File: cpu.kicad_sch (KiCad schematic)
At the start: 32 parts, among them J10 Skedd, J13 Boot, J7 USB_C_Receptacle_16P, U4 STM32H503KBUx

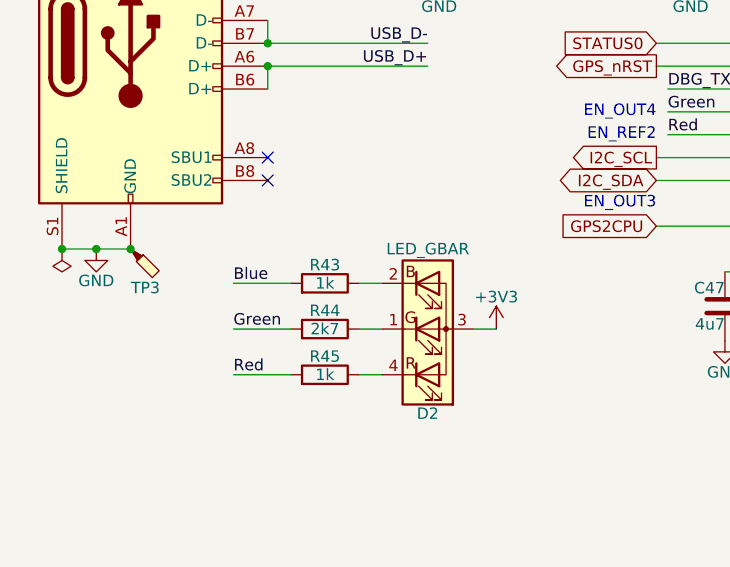
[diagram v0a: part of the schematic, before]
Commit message: Make all the LED resistors 0603 & adjust values.
Move the LED inwards so it doesn't overhang.
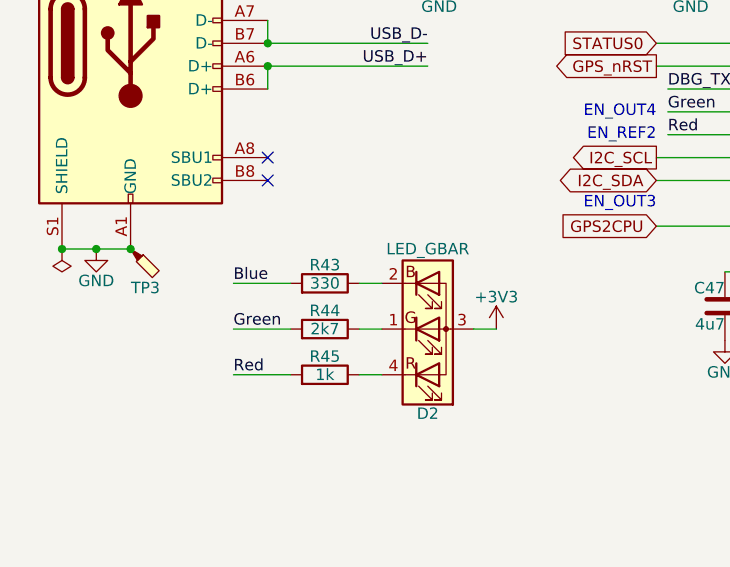
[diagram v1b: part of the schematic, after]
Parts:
- R43: value 1k -> 330; footprint Resistor_SMD:R_0402_1005Metric -> Resistor_SMD:R_0603_1608Metric; LCSC C11702 -> C23138
- R45: footprint Resistor_SMD:R_0402_1005Metric -> Resistor_SMD:R_0603_1608Metric; LCSC C11702 -> C21190

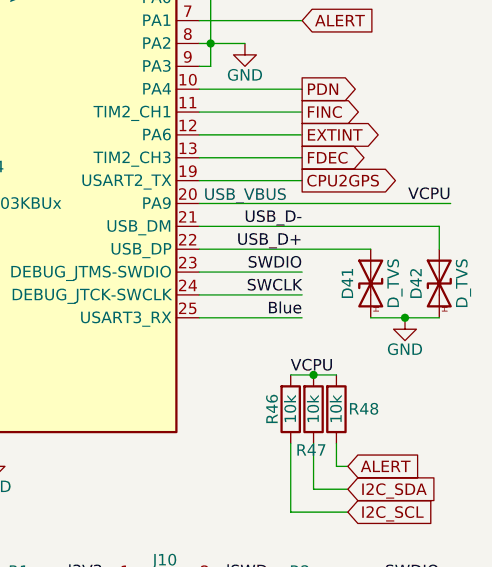
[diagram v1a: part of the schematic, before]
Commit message: Add LCSC part numbers for a few items.
Don't 'exclude from BOM' things we want to assemble.
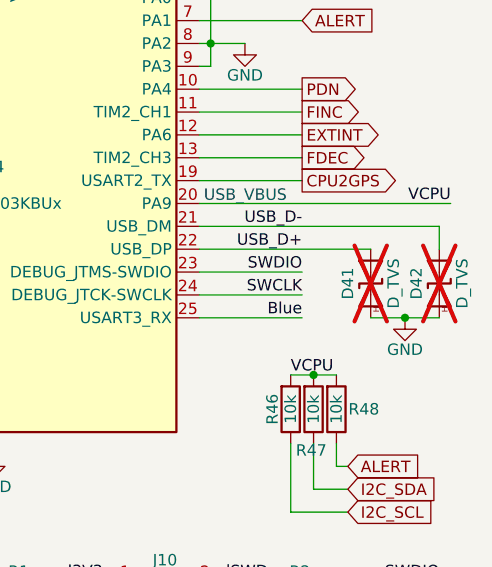
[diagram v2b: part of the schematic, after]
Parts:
- D41, D42: now not fitted
- J7: LCSC (none) -> C2765186; now in the parts list
- U4: now in the parts list

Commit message: Tweaks to python scripts.
Add part numbers for the LED and 470nF C0G capacitor.
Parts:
- D2: LCSC (none) -> C284951

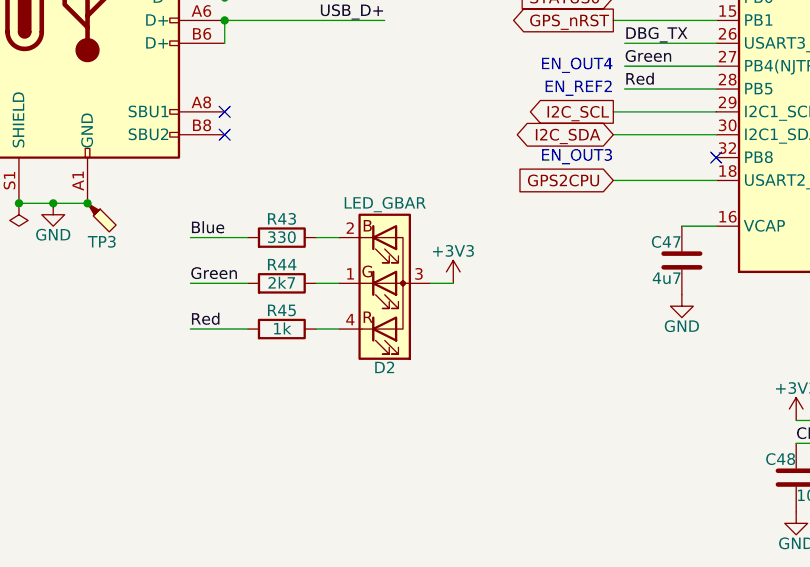
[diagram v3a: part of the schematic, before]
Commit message: Instead, switch to a RGB LED footprint from Paul Elliot.
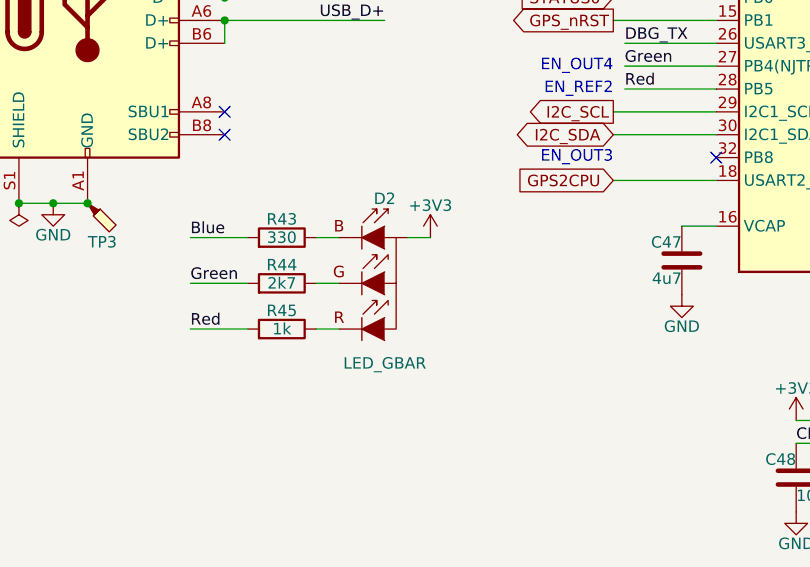
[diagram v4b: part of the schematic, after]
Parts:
- D2: footprint Parts:LED-QPLB615-RGB -> Parts:LED_RGB_SIDE; symbol Device:LED_GBAR -> Parts:LED_RGB_SIDE; LCSC C284951 -> C389528; now in the parts list
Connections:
- net +3V3: now also D2.1 (C); no longer D2.3 (A)
- net at R44.1: now also D2.3 (G); no longer D2.1 (GK)

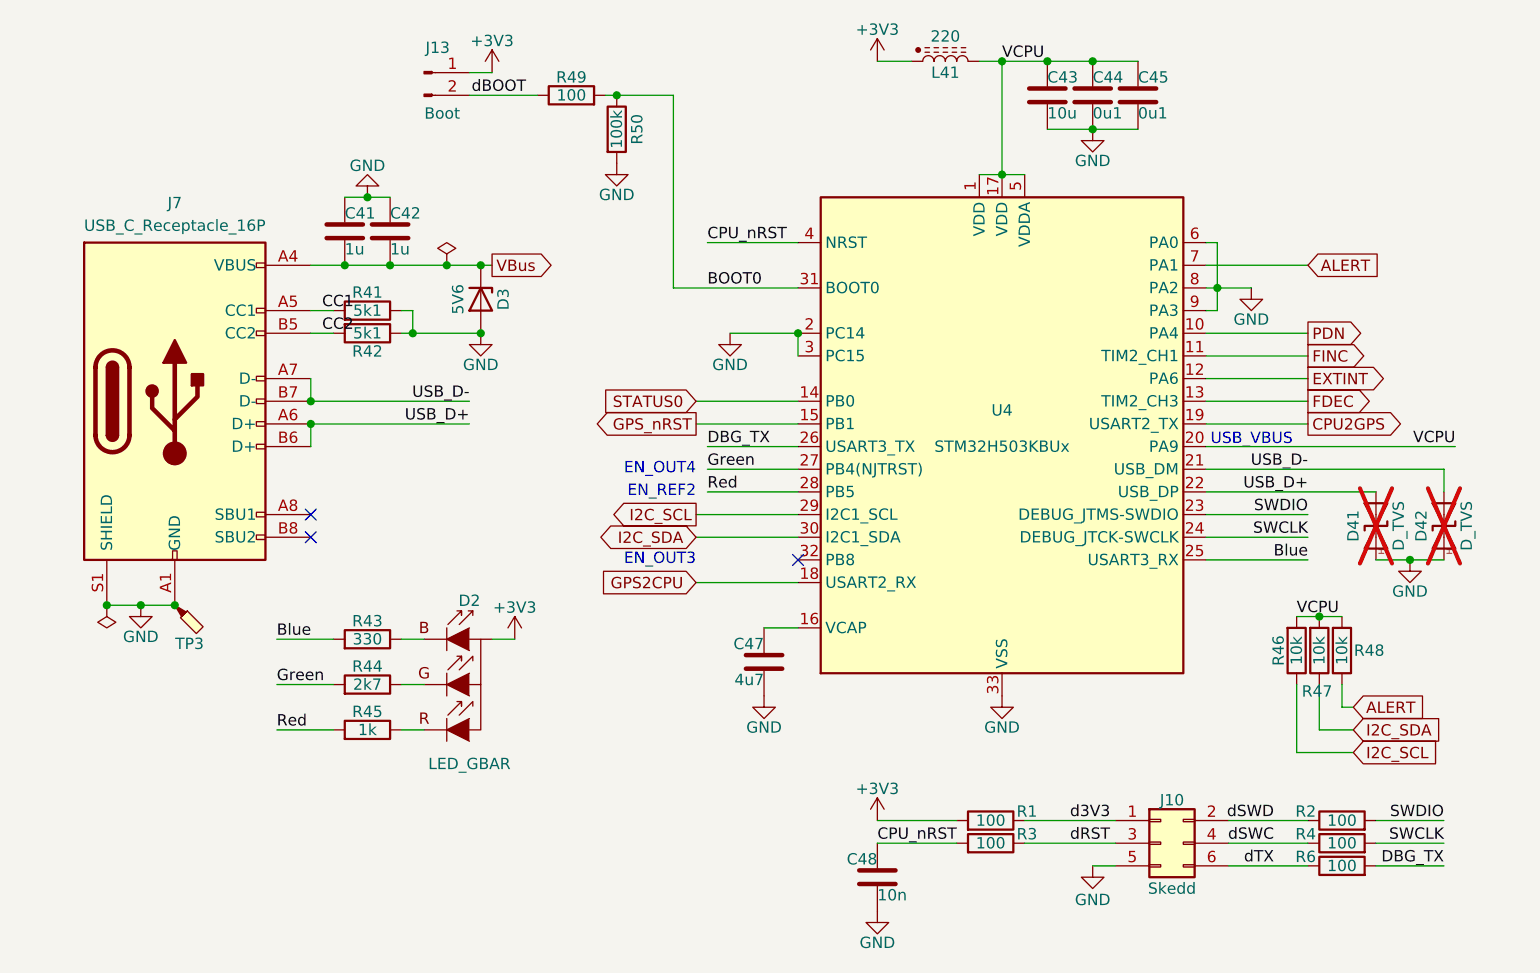
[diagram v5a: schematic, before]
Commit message: FPGA in, layout mostly updated.
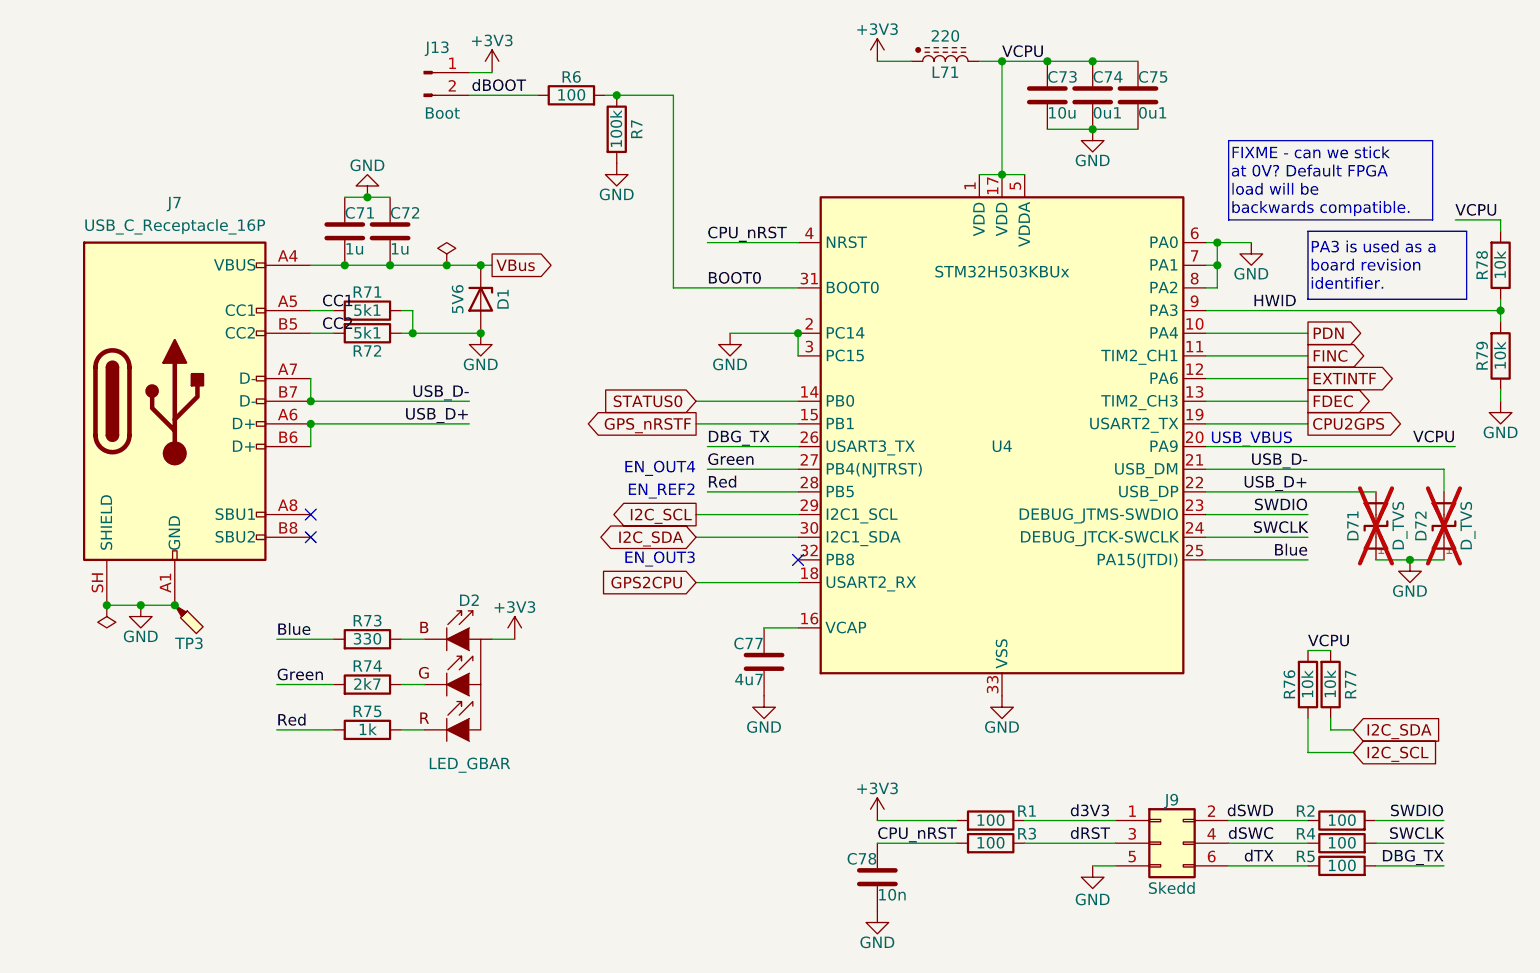
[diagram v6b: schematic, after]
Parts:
- removed R48: 10k, Resistor_SMD:R_0402_1005Metric, symbol Device:R
- added R78, R79: 10k, Resistor_SMD:R_0402_1005Metric, symbol Device:R
- renumbered C41 to C71, C42 to C72, C43 to C73, C44 to C74, C45 to C75, C47 to C77, C48 to C78, D3 to D1, D41 to D71, D42 to D72, J10 to J9, L41 to L71, R6 to R5, R49 to R6, R50 to R7, R41 to R71, R42 to R72, R43 to R73, R44 to R74, R45 to R75, R46 to R76, R47 to R77
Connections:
- net ALERT is gone; now on net GND: U4.7 (PA1)
- net GND: now also J7.SH (SHIELD), R79.1; no longer J7.S1 (SHIELD), U4.9 (PA3)
- net VCPU: now also R78.2
- net EXTINT renamed EXTINTF
- net GPS_nRST renamed GPS_nRSTF
- new net HWID: R78.1, R79.2, U4.9 (PA3)
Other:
- moved on the sheet: R76, R77

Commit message: Layout down
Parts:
- removed D71, D72: D_TVS, Parts:HHS_0402, symbol Parts:D_TVS
- added C73: 1u, Capacitor_SMD:C_0402_1005Metric, symbol Device:C
- added U71: USBLC6-2SC6, Parts:SOT-666-6, symbol Power_Protection:USBLC6-2SC6
- C71, C72, C77, C78, R1, R2, R3, R4, R5, R6, R7, R71, R72, R73, R74, R75, R76, R77, R78, R79: Stock (none) -> Basic
- C74: renamed from C73; Stock (none) -> Basic
- C75: renamed from C74; Stock (none) -> Basic
- C76: renamed from C75; Stock (none) -> Basic
- D1: Stock (none) -> Prom
- D2: Stock (none) -> 9; now left out of the parts list
- J13, J9, TP3: Stock (none) -> N/A
- J7: Stock (none) -> Heaps; now left out of the parts list
- L71: value 220 -> 120; Stock (none) -> Basic
- U4: Stock (none) -> 2; now left out of the parts list
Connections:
- net GND: now also C73.1, U71.2 (GND)
- net USB_D+: now also U71.3 (I/O2), U71.4 (I/O2)
- net USB_D-: now also U71.1 (I/O1), U71.6 (I/O1)
- net VBus: now also C73.2, U71.5 (VBUS)
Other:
- moved on the sheet: C71, C72, D1, J7, R71, R72, TP3

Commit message: Ordered.
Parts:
- C75, C76: value 0u1 -> 1u; LCSC C307331 -> C52923
- U71: now left out of the parts list
